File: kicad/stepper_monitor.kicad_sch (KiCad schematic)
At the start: 63 parts, among them J1 Conn_01x04_Pin, J2 Conn_01x04_Pin, J3 Conn_01x02_Pin, J4 USB_C_Receptacle_USB2.0, J5 JTAG, M1 Motor-simple_stepper_motor_an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, Q1 MMDT2222A, SW1 SW_Push, U1 5V, U2 CP2102N-A01-GQFN28, U3 AMS1117-3.3, U4 CC6920BSO-5A, U5 CC6920BSO-5A, U6 ESP32-WROOM-32U-N4

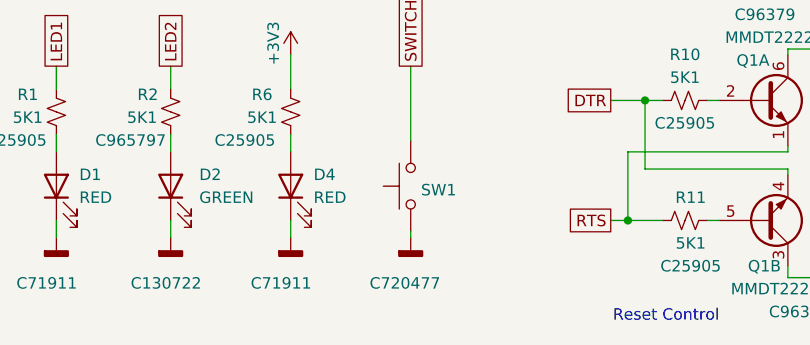
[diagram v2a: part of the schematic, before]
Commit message: JLC basic part button
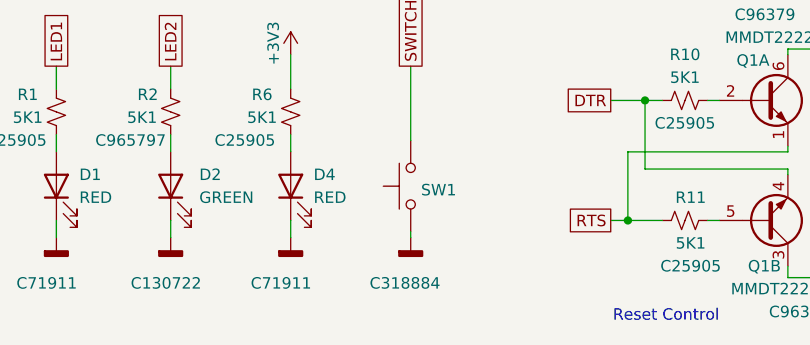
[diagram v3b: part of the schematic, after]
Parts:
- SW1: footprint stepper_monitor:SW_Push_SPST_NO_Alps_SKRK -> Button_Switch_SMD:SW_SPST_TL3342; LCSC C720477 -> C318884
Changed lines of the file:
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@@
       (effects (font (size 1.27 1.27)) (justify right) hide)
     )
-    (property "Footprint" "stepper_monitor:SW_Push_SPST_NO_Alps_SKRK" (at 62.23 175.895 0)
+    (property "Footprint" "Button_Switch_SMD:SW_SPST_TL3342" (at 62.23 175.895 0)
       (effects (font (size 1.27 1.27)) hide)
     )
@@
       (effects (font (size 1.27 1.27)) hide)
     )
-    (property "LCSC" "C720477" (at 66.675 186.69 90)
+    (property "LCSC" "C318884" (at 66.675 186.69 90)
       (effects (font (size 1.27 1.27)))
     )

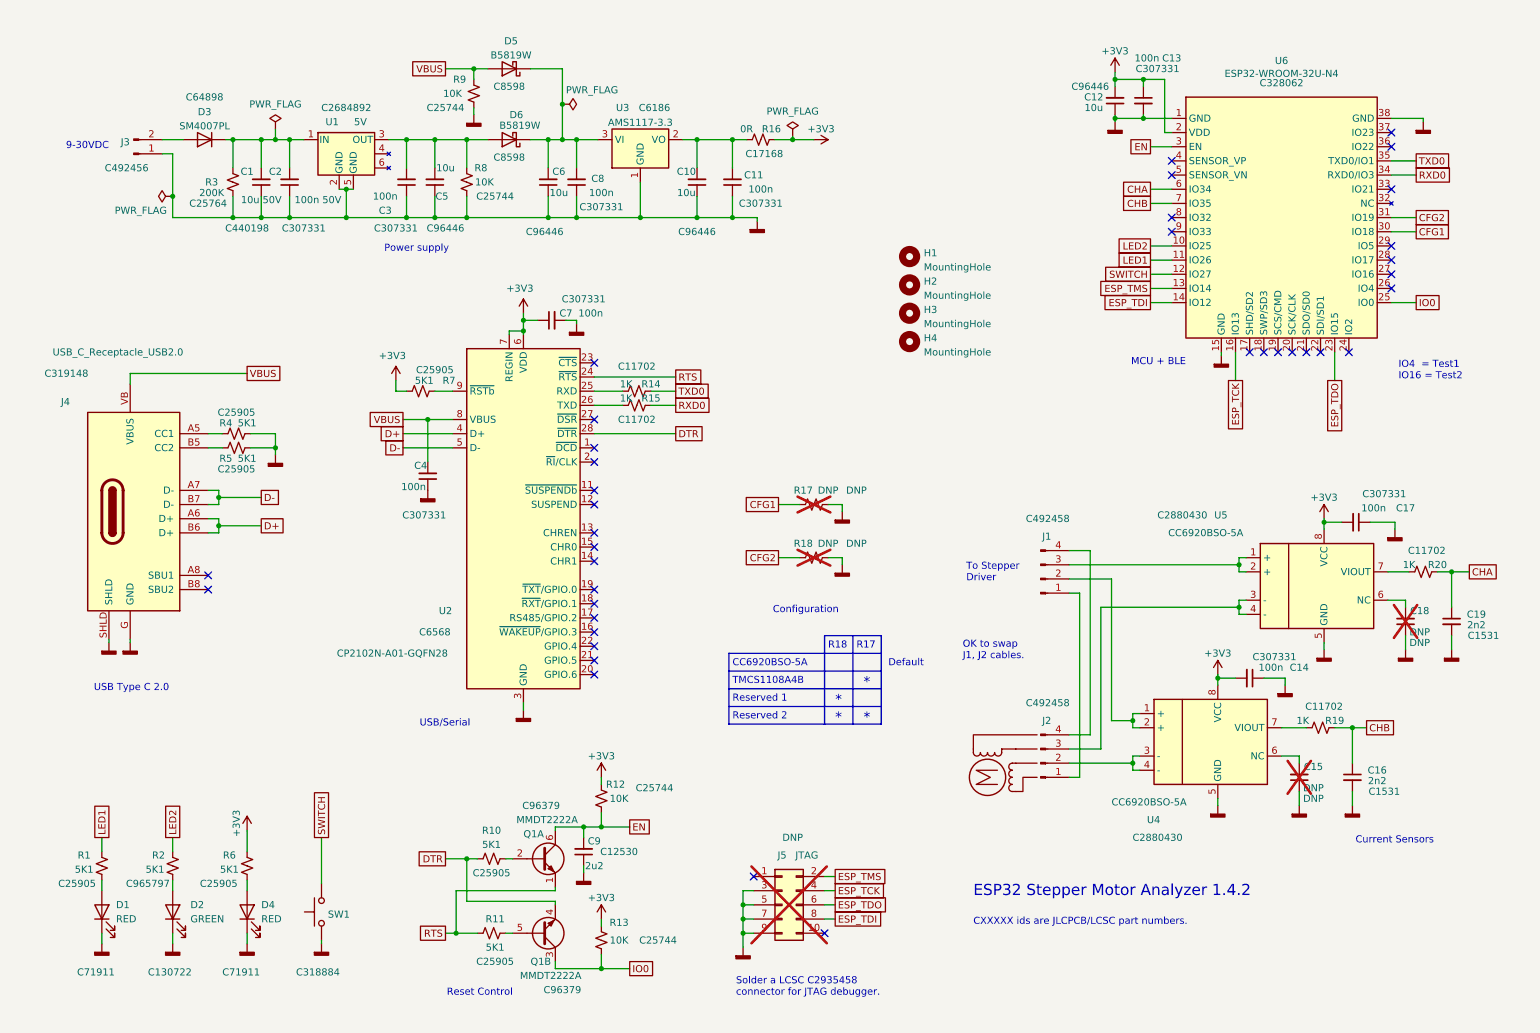
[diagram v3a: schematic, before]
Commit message: Connected VZCR pin from CC6920BSO. Added big scope test points. Ignored local file.
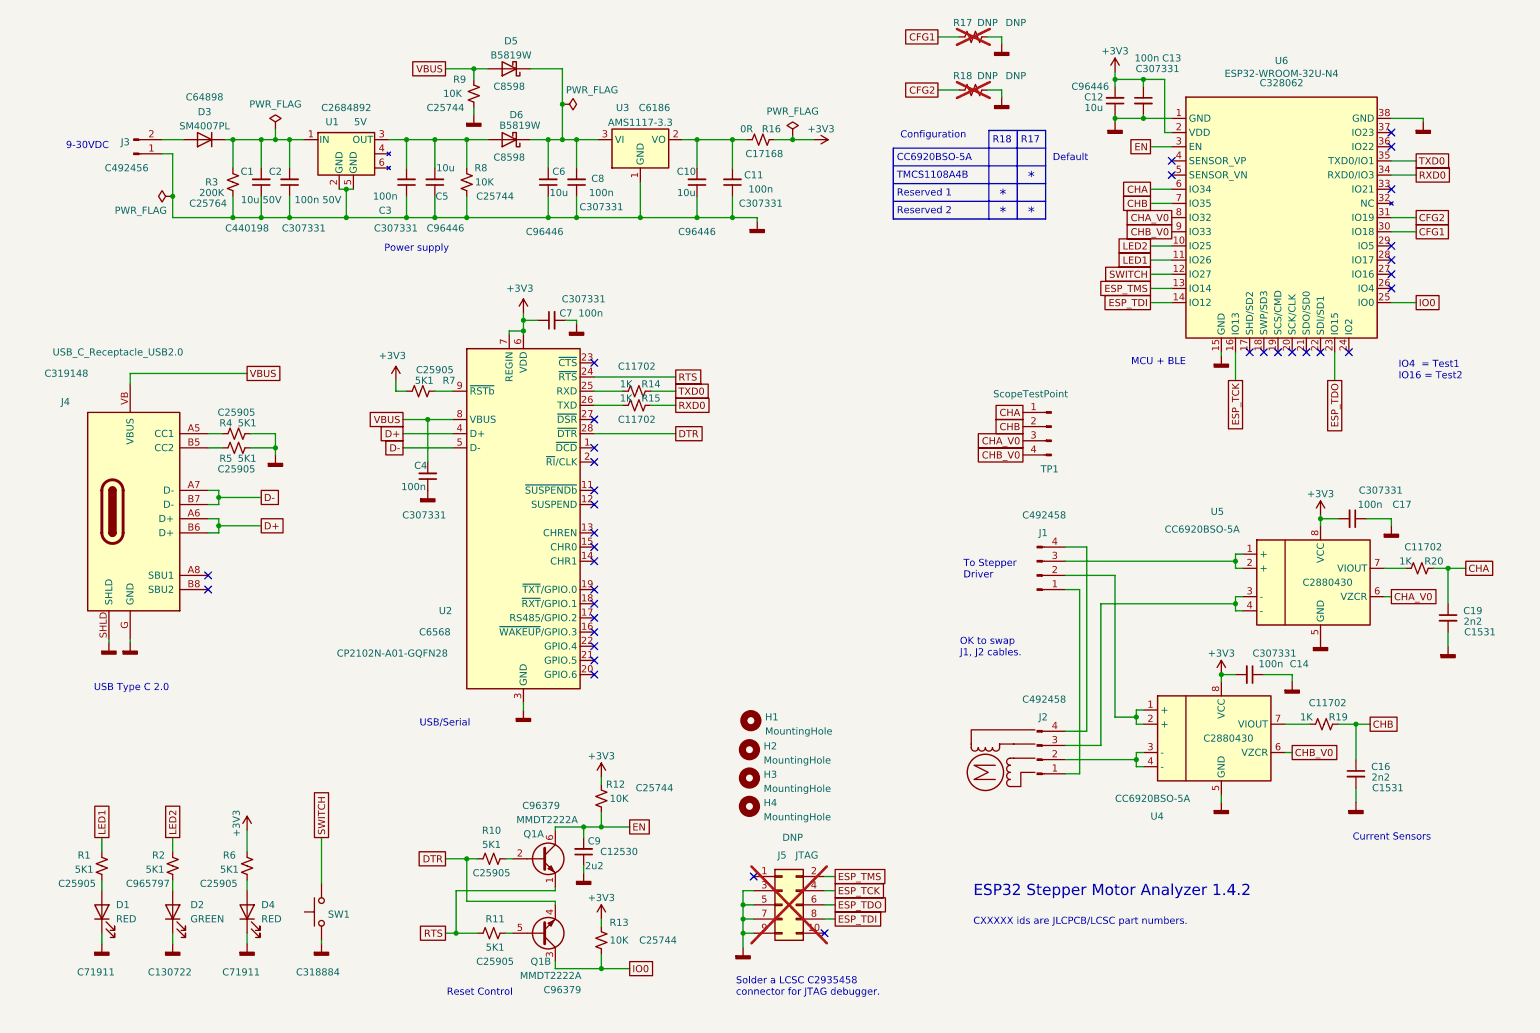
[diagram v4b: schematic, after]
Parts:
- removed C15, C18: DNP, Capacitor_SMD:C_0402_1005Metric, symbol Device:C_Small
- added TP1: ScopeTestPoint, Connector_PinHeader_2.54mm:PinHeader_1x04_P2.54mm_Vertical, symbol Connector:Conn_01x04_Pin
- U4, U5: footprint stepper_monitor:SOIC-8_3.9x4.9mm_P1.27mm -> Package_SO:SOIC-8_3.9x4.9mm_P1.27mm; symbol stepper_monitor:ACS70331_soic8 -> stepper_monitor:CC6920BSO_soic8
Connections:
- net CHA: now also TP1.1 (Pin_1)
- net CHB: now also TP1.2 (Pin_2)
- net CHA_V0: now reaches U6.8 (IO32)
- net CHA_V0: now also U5.6 (VZCR), TP1.3 (Pin_3)
- net CHB_V0: now reaches U6.9 (IO33)
- net CHB_V0: now also U4.6 (VZCR), TP1.4 (Pin_4)
- no-connect marks 38 -> 36
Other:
- moved on the sheet: C14, C16, C17, C19, H1, H2, H3, H4, J1, J2, R17, R18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

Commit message: Rerouted everything. Basic part LEDs. 6 pin connector. Smaller footprint. Shorter routes
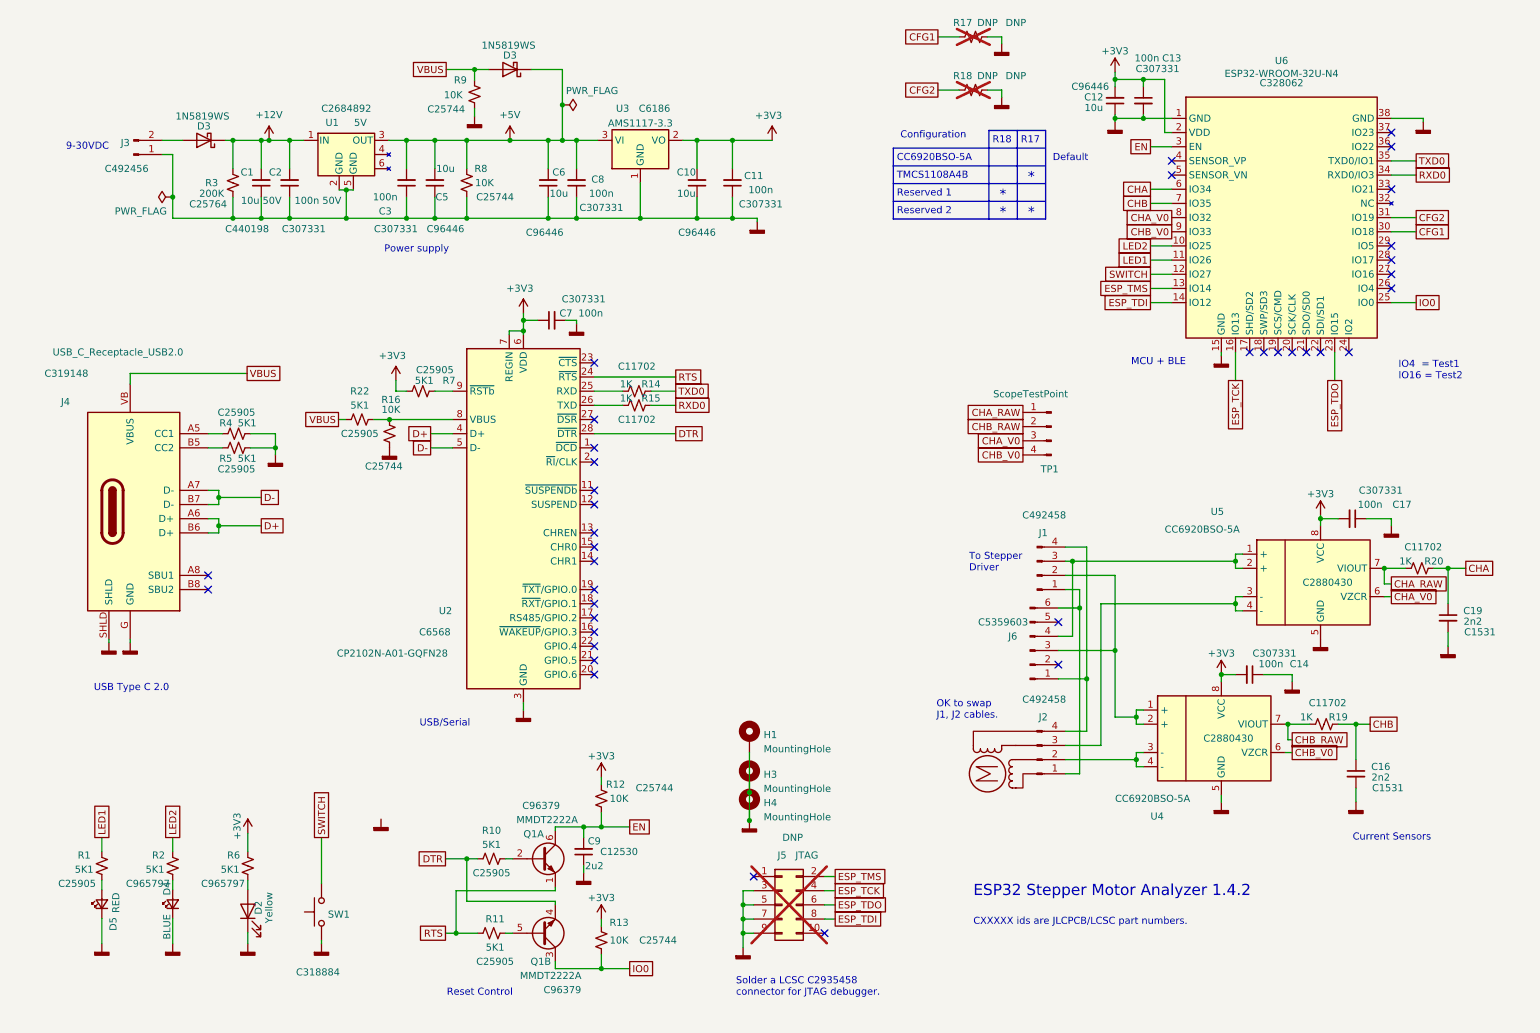
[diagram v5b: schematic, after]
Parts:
- removed C4: 100n, Capacitor_SMD:C_0402_1005Metric, symbol Device:C_Small
- removed D1, D4: RED, stepper_monitor:LED_0402_1005Metric_Pad0.77x0.64mm_HandSolder, symbol Device:LED
- removed D3: SM4007PL, stepper_monitor:D2_SOD-123, symbol Diode:1N4005
- removed D5, D6: B5819W, stepper_monitor:D_SOD-123, symbol Device:D_Schottky
- removed H2: MountingHole, MountingHole:MountingHole_3.2mm_M3_Pad_Via, symbol Mechanical:MountingHole
- added D3 (x2): 1N5819WS, Diode_SMD:D_SOD-323, symbol Diode:1N5819
- added D4: BLUE, LED_SMD:LED_0603_1608Metric, symbol Device:LED_Small
- added D5: RED, LED_SMD:LED_0603_1608Metric, symbol Device:LED_Small
- added J6: Conn_01x04_Pin, Connector_JST:JST_PH_B6B-PH-K_1x06_P2.00mm_Vertical, symbol Connector:Conn_01x06_Pin
- added R22: 5K1, Resistor_SMD:R_0402_1005Metric, symbol Device:R_Small_US
- D2: value GREEN -> Yellow; footprint stepper_monitor:LED_0402_1005Metric_Pad0.77x0.64mm_HandSolder -> LED_SMD:LED_0603_1608Metric; LCSC C130722 -> C72038
- H1, H3, H4: symbol Mechanical:MountingHole -> Mechanical:MountingHole_Pad
- R16: value 0R -> 10K; LCSC C17168 -> C25744
- R6: LCSC C25905 -> C965797
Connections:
- net +3V3: now also C10.2, C11.2, U3.2 (VO); no longer R16.1
- net CHA: no longer TP1.1 (Pin_1)
- net CHB: no longer TP1.2 (Pin_2)
- net GNDD: now also H1.1, H3.1, H4.1, R16.1, D4.1 (K), D5.1 (K)
- net VBUS: now also D3.2 (A), R22.1; no longer U2.8 (VBUS)
- net +5V: now reaches C6.2, C8.2, U3.3 (VI)
- net +5V: now also C3.2, C5.2, R8.2, U1.3 (OUT), D3.1 (K)
- net at R6.1: now also D2.2 (A)
- net at R1.1: now also D5.2 (A)
- net at R2.1: now also D4.2 (A); no longer D2.2 (A)
- net +12V: now reaches C1.2, C2.2, R3.1, U1.1 (IN)
- net +12V: now also D3.1 (K)
- net CHA_RAW: now reaches R20.2, U5.7 (VIOUT)
- net CHA_RAW: now also TP1.1 (Pin_1)
- net at J3.2 (Pin_2): now also D3.2 (A)
- net at J1.1 (Pin_1), J2.1 (Pin_1): now also J6.6 (Pin_6)
- net at J1.4 (Pin_4), J2.4 (Pin_4): now also J6.1 (Pin_1)
- net at J1.2 (Pin_2), U4.1 (+), U4.2 (+): now also J6.3 (Pin_3)
- net CHB_RAW: now reaches R19.2, U4.7 (VIOUT)
- net CHB_RAW: now also TP1.2 (Pin_2)
- net at J1.3 (Pin_3), U5.1 (+), U5.2 (+): now also J6.4 (Pin_4)
- new net: R16.2, R22.2, U2.8 (VBUS)
- no-connect marks 36 -> 38

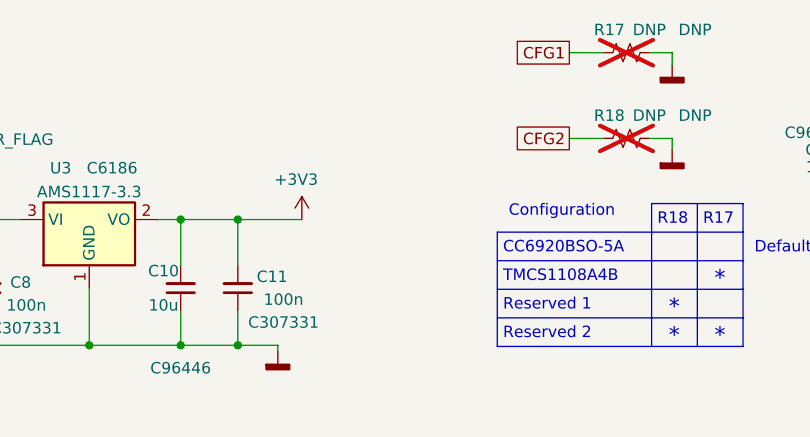
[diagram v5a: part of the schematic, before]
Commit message: Added 5V dupoint pins
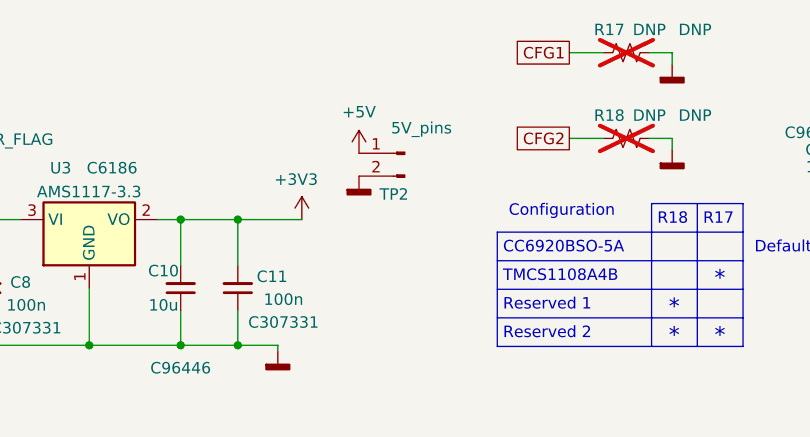
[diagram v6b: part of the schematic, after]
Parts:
- added TP2: 5V_pins, Connector_PinHeader_2.54mm:PinHeader_1x02_P2.54mm_Vertical, symbol Connector:Conn_01x02_Pin
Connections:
- net +5V: now also TP2.1 (Pin_1)
- net GNDD: now also TP2.2 (Pin_2)
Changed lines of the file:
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@@
+    )
+  )
+  (symbol (lib_id "power:+5V") (at 154.432 30.226 0) (unit 1)
+    (in_bom yes) (on_board yes) (dnp no) (fields_autoplaced)
+    (property "Reference" "#PWR039" (at 154.432 34.036 0)
+      (effects (font (size 1.27 1.27)) hide)
+    )
+    (property "Value" "+5V" (at 154.432 25.654 0)
+      (effects (font (size 1.27 1.27)))
+    )
+    (property "Footprint" "" (at 154.432 30.226 0)
+      (effects (font (size 1.27 1.27)) hide)
+    )
+    (property "Datasheet" "" (at 154.432 30.226 0)
+      (effects (font (size 1.27 1.27)) hide)
+    )
+    (pin "1")
+    (instances
+      (project "stepper_monitor"
+        (path "/ab9a1617-734a-47a3-94aa-b13da0ec18df"
+          (reference "#PWR039") (unit 1)
+        )
+      )
     )
   )
@@
         (path "/ab9a1617-734a-47a3-94aa-b13da0ec18df"
           (reference "R14") (unit 1)
+        )
+      )
+    )
+  )
+  (symbol (lib_id "power:GNDD") (at 154.432 32.766 0) (unit 1)
+    (in_bom yes) (on_board yes) (dnp no)
+    (property "Reference" "#PWR040" (at 154.432 39.116 0)
+      (effects (font (size 1.27 1.27)) hide)
+    )
+    (property "Value" "GNDD" (at 154.5336 36.703 0)
+      (effects (font (size 1.27 1.27)) hide)
+    )
+    (property "Footprint" "" (at 154.432 32.766 0)
+      (effects (font (size 1.27 1.27)) hide)
+    )
+    (property "Datasheet" "" (at 154.432 32.766 0)
+      (effects (font (size 1.27 1.27)) hide)
+    )
+    (pin "1")
+    (instances
+      (project "stepper_monitor"
+        (path "/ab9a1617-734a-47a3-94aa-b13da0ec18df"
+          (reference "#PWR040") (unit 1)
         )
       )
@@
         )
       )
+    )
+  )
+  (symbol (lib_id "Connector:Conn_01x02_Pin") (at 159.512 30.226 0) (mirror y) (unit 1)
+    (in_bom yes) (on_board yes) (dnp no)
+    (property "Reference" "TP2" (at 156.718 34.798 0)
+      (effects (font (size 1.27 1.27)) (justify right))
+    )
+    (property "Value" "5V_pins" (at 157.988 27.432 0)
+      (effects (font (size 1.27 1.27)) (justify right))
+    )
+    (property "Footprint" "Connector_PinHeader_2.54mm:PinHeader_1x02_P2.54mm_Vertical" (at 159.512 30.226 0)
+      (effects (font (size 1.27 1.27)) hide)
+    )
+    (property "Datasheet" "~" (at 159.512 30.226 0)
+      (effects (font (size 1.27 1.27)) hide)
+    )
+    (property "LCSC" "" (at 158.242 41.021 0)
+      (effects (font (size 1.27 1.27)))
+    )
+    (pin "1")
+    (pin "2")
+    (instances
+      (project "stepper_monitor"
+        (path "/ab9a1617-734a-47a3-94aa-b13da0ec18df"
+          (reference "TP2") (unit 1)
+        )
+      )

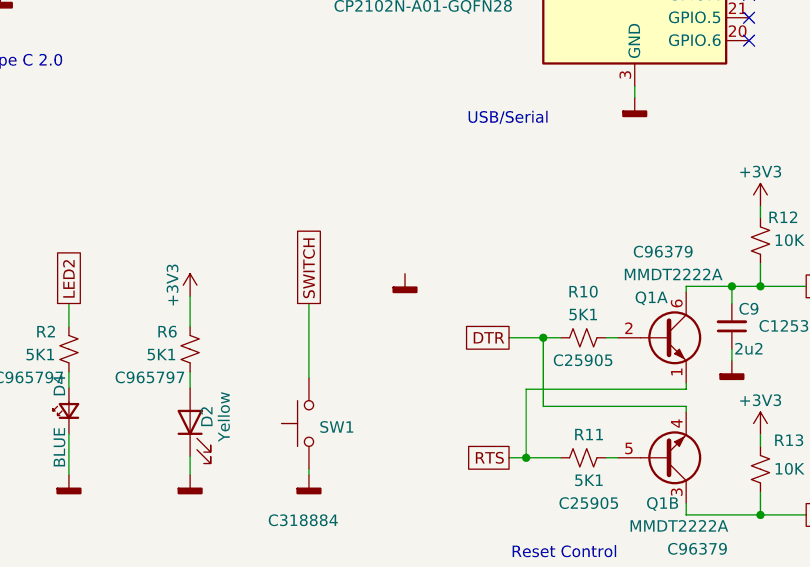
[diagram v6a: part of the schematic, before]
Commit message: Using "official" espressif footprints
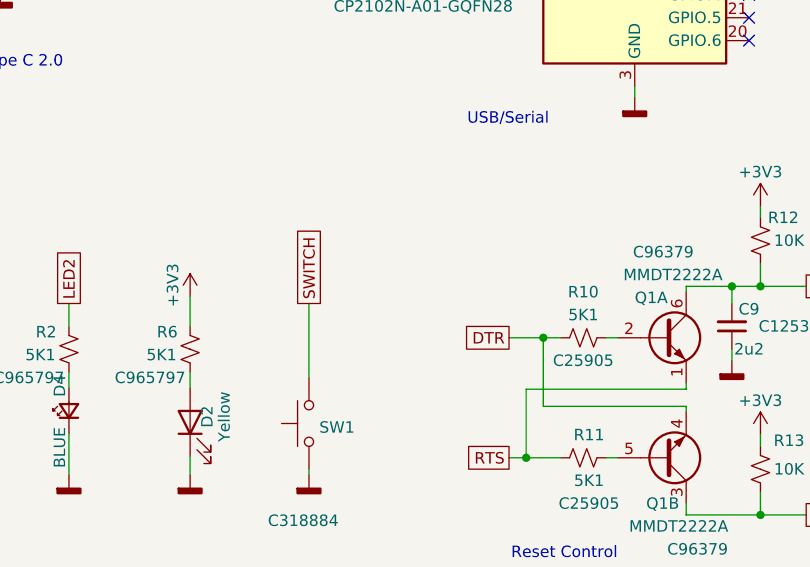
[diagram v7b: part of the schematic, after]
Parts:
- U6: footprint stepper_monitor:ESP32-WROOM-32U -> stepper_monitor:ESP32-WROOM-32UE
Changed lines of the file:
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@@
       (effects (font (size 1.27 1.27)))
     )
-    (property "Footprint" "stepper_monitor:ESP32-WROOM-32U" (at 238.76 23.495 0)
+    (property "Footprint" "stepper_monitor:ESP32-WROOM-32UE" (at 238.76 23.495 0)
       (effects (font (size 1.27 1.27)) hide)
     )
@@
         )
       )
-    )
-  )
-  (symbol (lib_id "power:GNDD") (at 77.978 159.258 0) (unit 1)
-    (in_bom yes) (on_board yes) (dnp no)
-    (property "Reference" "#PWR020" (at 77.978 165.608 0)
-      (effects (font (size 1.27 1.27)) hide)
-    )
-    (property "Value" "GNDD" (at 78.0796 163.195 0)
-      (effects (font (size 1.27 1.27)) hide)
-    )
-    (property "Footprint" "" (at 77.978 159.258 0)
-      (effects (font (size 1.27 1.27)) hide)
-    )
-    (property "Datasheet" "" (at 77.978 159.258 0)
-      (effects (font (size 1.27 1.27)) hide)
-    )
-    (pin "1")
-    (instances
-      (project "stepper_monitor"
-        (path "/ab9a1617-734a-47a3-94aa-b13da0ec18df"
-          (reference "#PWR020") (unit 1)
-        )
-      )
